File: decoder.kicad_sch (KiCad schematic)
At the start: 35 parts, among them U1 SAA7114H, X1 ACHL-24.576MHZ-EK

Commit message: minor cleanup, addition of notes
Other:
- note added: "Expansion port unused in this design."
- note added: "TODO: determine whether I2C port supports address auto-increment (like the SAA7182A does)"
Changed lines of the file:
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@@
     (stroke (width 0) (type default))
   )
-  (text_box "Note: ITRDY contains internal pullup"
+  (text_box "NOTE: ITRDY contains internal pullup"
     (at 224.79 92.71 0) (size 22.5425 5.08)
     (stroke (width 0) (type default))
@@
     (effects (font (size 1.27 1.27)) (justify left top))
   )
-  (text_box "Note: do not populate, SAA7114H contains internal pulldown"
-    (at 224.79 123.19 0) (size 24.13 7.62)
+  (text_box "NOTE: do not populate, SAA7114H contains internal pulldown"
+    (at 224.79 123.19 0) (size 25.4 7.62)
     (stroke (width 0) (type default))
     (fill (type none))
     (effects (font (size 1.27 1.27)) (justify left top))
   )
-  (text_box "Note: added decoupling cap for VDD(XTAL)"
+  (text_box "NOTE: added decoupling cap for VDD(XTAL)"
     (at 151.13 161.29 0) (size 17.78 7.62)
     (stroke (width 0) (type default))
@@
     (effects (font (size 1.27 1.27)) (justify left top))
   )
-  (text_box "Note: POR circuit added for CE"
-    (at 90.17 156.21 0) (size 19.05 5.08)
+  (text_box "NOTE: POR circuit added for CE"
+    (at 87.63 157.48 0) (size 21.59 5.08)
     (stroke (width 0) (type default))
     (fill (type none))
@@
   )
   (text_box "NOTE: major differences from Marcus's circuit and this one include:\n1. Marcus used 22R for each of the inputs, I used 18R per datasheet;\n** 2. Marcus connected his S-VIDEO signal to AI12 and AI22, I connected mine to AI21 and AI22, I'll need to double-check the datasheet on this, it might be an error\n3. Marcus had an AGND and DGND, this board only has a single (non-split) GND; and\n4. This circuit does not populate the ALRCLK pull-down to GND, as there is already an internal pulldown per datasheet."
-    (at 205.74 144.78 0) (size 72.39 19.05)
+    (at 210.82 144.78 0) (size 72.39 19.05)
     (stroke (width 0) (type default))
     (fill (type none))
@@
     (effects (font (size 1.27 1.27)) (justify left bottom))
   )
+  (text "TODO: determine whether I2C port\nsupports address auto-increment\n(like the SAA7182A does)"
+    (at 74.93 29.21 0)
+    (effects (font (size 1.27 1.27)) (justify left bottom))
+  )
   (text "TODO: does ITRI need connecting?\n(I think no, because \"enable under\nsoftware control\" per datasheet)"
     (at 224.79 106.68 0)
@@
   )
   (text "TODO: does XTRI need connecting?\n(I think no, because \"enable under\nsoftware control\" per datasheet)"
-    (at 58.42 53.34 0)
+    (at 57.15 53.34 0)
     (effects (font (size 1.27 1.27)) (justify left bottom))
   )
+  (text "Expansion port unused in this design." (at 57.15 63.5 0)
+    (effects (font (size 1.27 1.27)) (justify left bottom))
+  )

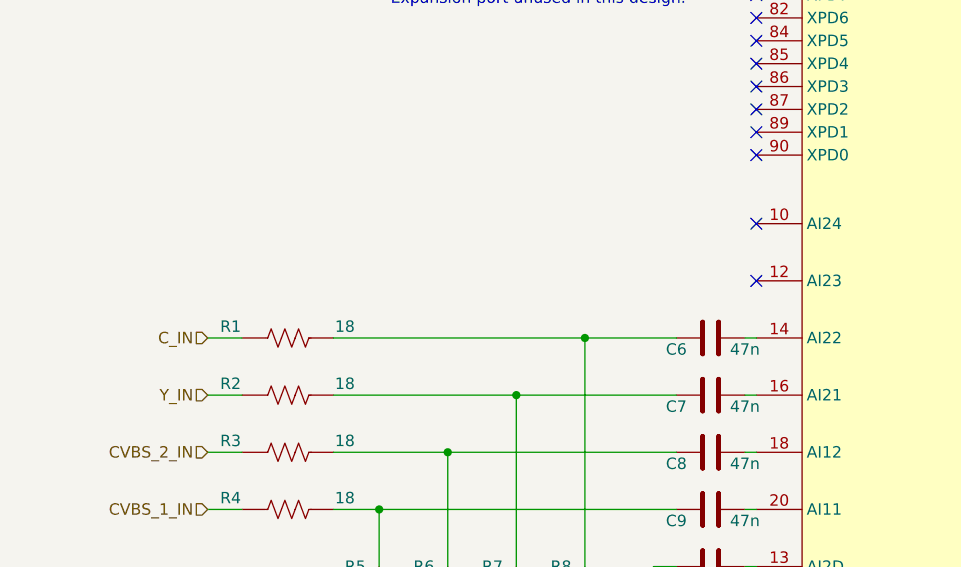
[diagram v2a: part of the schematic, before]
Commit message: added footprints for large ICs
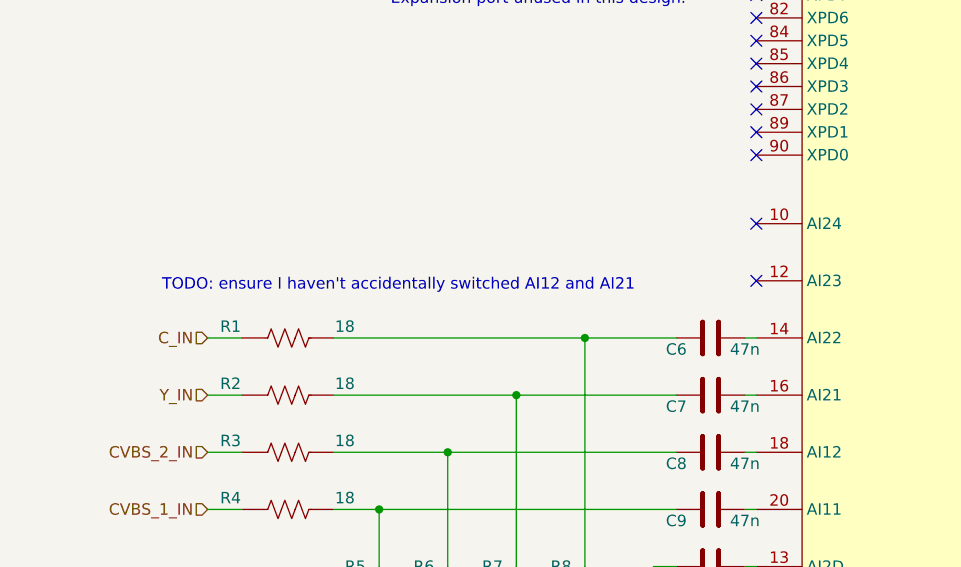
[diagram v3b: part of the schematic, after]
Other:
- note added: "TODO: ensure I haven't accidentally switched AI12 and AI21"
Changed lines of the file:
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@@
+    (effects (font (size 1.27 1.27)) (justify left bottom))
+  )
+  (text "TODO: ensure I haven't accidentally switched AI12 and AI21"
+    (at 31.75 95.25 0)
     (effects (font (size 1.27 1.27)) (justify left bottom))
   )

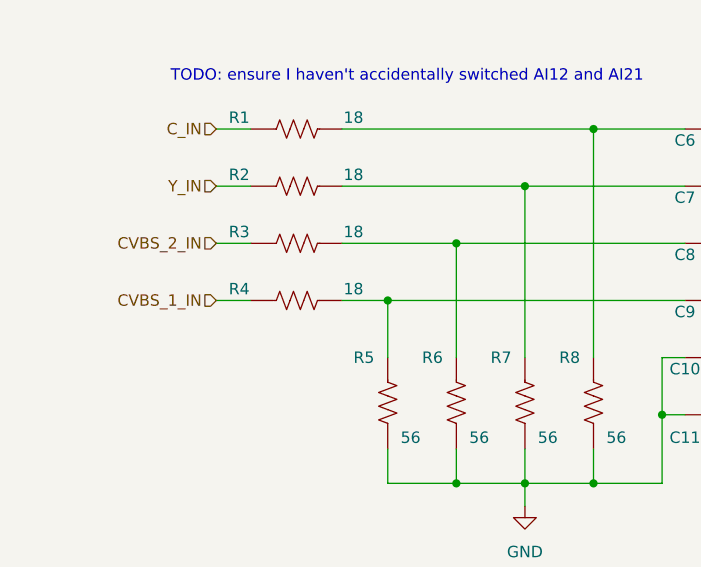
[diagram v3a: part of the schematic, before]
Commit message: resistor footprint added
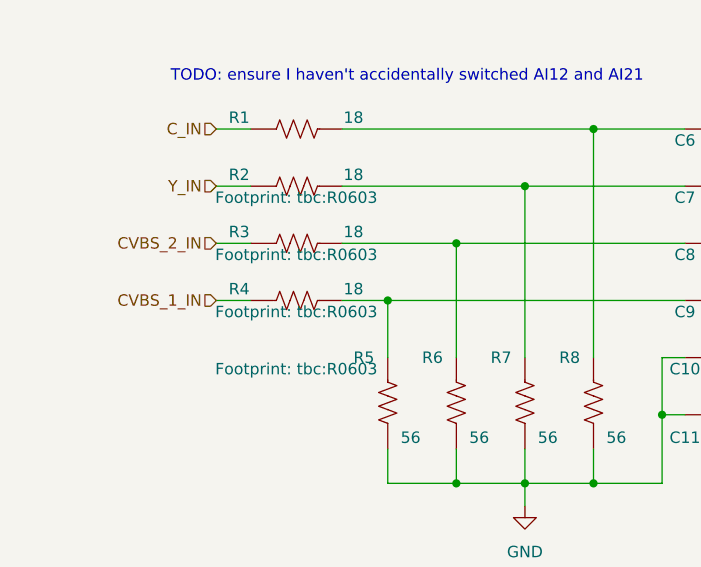
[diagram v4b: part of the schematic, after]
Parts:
- R1, R10, R2, R3, R4, R5, R6, R7, R8, R9: footprint (none) -> tbc:R0603
- U1: footprint (none) -> tbc:LQFP100_14x14x1.4mm_Pitch0.5mm
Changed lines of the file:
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@@
       (effects (font (size 1.27 1.27)))
     )
-    (property "Footprint" "" (at 29.21 120.65 0)
-      (effects (font (size 1.27 1.27)) hide)
+    (property "Footprint" "tbc:R0603" (at 45.72 120.65 0) (show_name)
+      (effects (font (size 1.27 1.27)))
     )
     (property "Datasheet" "https://www.yageo.com/upload/media/product/products/datasheet/rchip/PYu-RC_Group_51_RoHS_L_12.pdf" (at 29.21 125.73 0) (show_name)
@@
       (effects (font (size 1.27 1.27)))
     )
-    (property "Footprint" "" (at 63.5 147.32 0)
+    (property "Footprint" "tbc:R0603" (at 63.5 130.81 0) (show_name)
       (effects (font (size 1.27 1.27)) hide)
     )
@@
       (effects (font (size 1.27 1.27)))
     )
-    (property "Footprint" "" (at 78.74 147.32 0)
+    (property "Footprint" "tbc:R0603" (at 78.74 130.81 0) (show_name)
       (effects (font (size 1.27 1.27)) hide)
     )
@@
       (effects (font (size 1.27 1.27)))
     )
-    (property "Footprint" "" (at 125.73 50.8 90)
+    (property "Footprint" "tbc:LQFP100_14x14x1.4mm_Pitch0.5mm" (at 153.67 166.37 0) (show_name)
       (effects (font (size 1.27 1.27)) hide)
     )
@@
       (effects (font (size 1.27 1.27)))
     )
-    (property "Footprint" "" (at 71.12 147.32 0)
+    (property "Footprint" "tbc:R0603" (at 71.12 130.81 0) (show_name)
       (effects (font (size 1.27 1.27)) hide)
     )
@@
       (effects (font (size 1.27 1.27)))
     )
-    (property "Footprint" "" (at 199.39 133.35 0)
+    (property "Footprint" "tbc:R0603" (at 215.9 133.35 0) (show_name)
       (effects (font (size 1.27 1.27)) hide)
     )
@@
       (effects (font (size 1.27 1.27)))
     )
-    (property "Footprint" "" (at 29.21 107.95 0)
-      (effects (font (size 1.27 1.27)) hide)
+    (property "Footprint" "tbc:R0603" (at 45.72 107.95 0) (show_name)
+      (effects (font (size 1.27 1.27)))
     )
     (property "Datasheet" "https://www.yageo.com/upload/media/product/products/datasheet/rchip/PYu-RC_Group_51_RoHS_L_12.pdf" (at 29.21 113.03 0) (show_name)
@@
       (effects (font (size 1.27 1.27)))
     )
-    (property "Footprint" "" (at 120.65 170.18 0)
+    (property "Footprint" "tbc:R0603" (at 120.65 153.67 0) (show_name)
       (effects (font (size 1.27 1.27)) hide)
     )
@@
       (effects (font (size 1.27 1.27)))
     )
-    (property "Footprint" "" (at 29.21 114.3 0)
-      (effects (font (size 1.27 1.27)) hide)
+    (property "Footprint" "tbc:R0603" (at 45.72 114.3 0) (show_name)
+      (effects (font (size 1.27 1.27)))
     )
     (property "Datasheet" "https://www.yageo.com/upload/media/product/products/datasheet/rchip/PYu-RC_Group_51_RoHS_L_12.pdf" (at 29.21 119.38 0) (show_name)
@@
       (effects (font (size 1.27 1.27)))
     )
-    (property "Footprint" "" (at 86.36 147.32 0)
+    (property "Footprint" "tbc:R0603" (at 86.36 130.81 0) (show_name)
       (effects (font (size 1.27 1.27)) hide)
     )
@@
       (effects (font (size 1.27 1.27)))
     )
-    (property "Footprint" "" (at 29.21 127 0)
-      (effects (font (size 1.27 1.27)) hide)
+    (property "Footprint" "tbc:R0603" (at 45.72 127 0) (show_name)
+      (effects (font (size 1.27 1.27)))
     )
     (property "Datasheet" "https://www.yageo.com/upload/media/product/products/datasheet/rchip/PYu-RC_Group_51_RoHS_L_12.pdf" (at 29.21 132.08 0) (show_name)

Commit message: added connector footprints
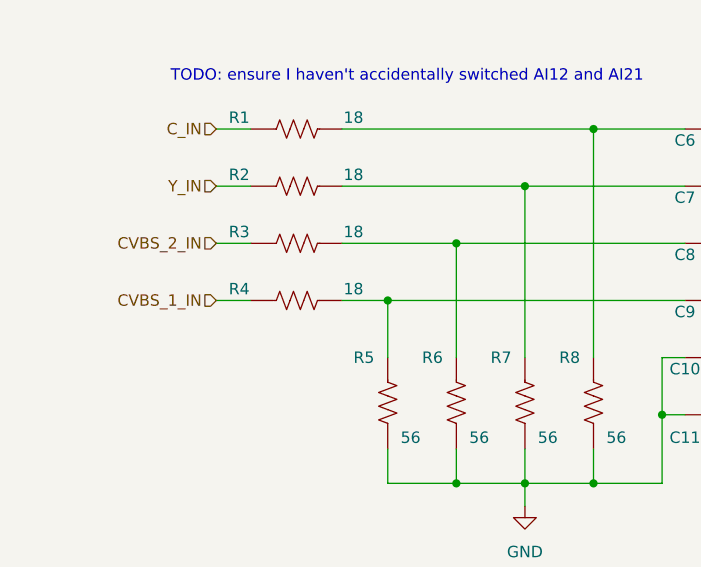
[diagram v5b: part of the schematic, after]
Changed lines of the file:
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@@
     )
     (property "Footprint" "tbc:R0603" (at 45.72 120.65 0) (show_name)
-      (effects (font (size 1.27 1.27)))
+      (effects (font (size 1.27 1.27)) hide)
     )
     (property "Datasheet" "https://www.yageo.com/upload/media/product/products/datasheet/rchip/PYu-RC_Group_51_RoHS_L_12.pdf" (at 29.21 125.73 0) (show_name)
@@
     )
     (property "Footprint" "tbc:R0603" (at 45.72 107.95 0) (show_name)
-      (effects (font (size 1.27 1.27)))
+      (effects (font (size 1.27 1.27)) hide)
     )
     (property "Datasheet" "https://www.yageo.com/upload/media/product/products/datasheet/rchip/PYu-RC_Group_51_RoHS_L_12.pdf" (at 29.21 113.03 0) (show_name)
@@
     )
     (property "Footprint" "tbc:R0603" (at 45.72 114.3 0) (show_name)
-      (effects (font (size 1.27 1.27)))
+      (effects (font (size 1.27 1.27)) hide)
     )
     (property "Datasheet" "https://www.yageo.com/upload/media/product/products/datasheet/rchip/PYu-RC_Group_51_RoHS_L_12.pdf" (at 29.21 119.38 0) (show_name)
@@
     )
     (property "Footprint" "tbc:R0603" (at 45.72 127 0) (show_name)
-      (effects (font (size 1.27 1.27)))
+      (effects (font (size 1.27 1.27)) hide)
     )
     (property "Datasheet" "https://www.yageo.com/upload/media/product/products/datasheet/rchip/PYu-RC_Group_51_RoHS_L_12.pdf" (at 29.21 132.08 0) (show_name)
